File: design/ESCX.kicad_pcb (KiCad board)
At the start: 4 copper layers, 100 x 100 mm, 130 parts, among them J1 SWD, J10 Screw_Terminal_01x03, J11 Screw_Terminal_01x02, J2 Conn_Coaxial, J8 HALL_ENC, J9 USB_C_Receptacle_USB2.0_16P, Q1 IRF7854, Q2 IRF7854, Q3 IRF7854, Q4 IRF7854, Q5 IRF7854, Q6 IRF7854, SW1 SENSOR_VOLTAGE, U1 STM32F40X_LQFP64, U2 LM3671, U3 DRV8301, U4 nRF24L01P, U5 AD8418, U6 AD8418, U7 AD8418, X1 8MHz, X2 16MHz

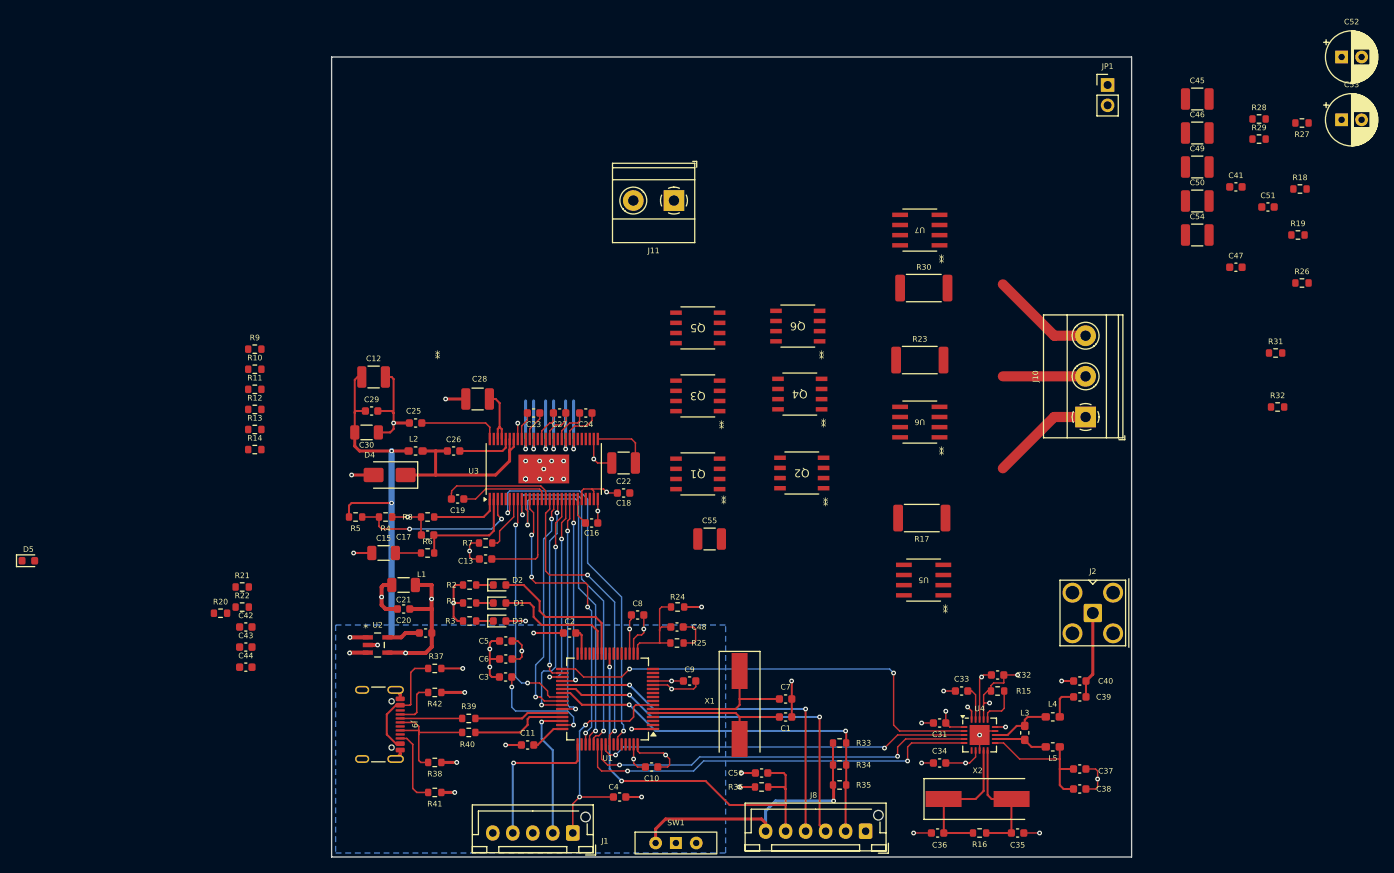
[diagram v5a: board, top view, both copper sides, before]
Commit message: Complete ruteo, menos plano GND2
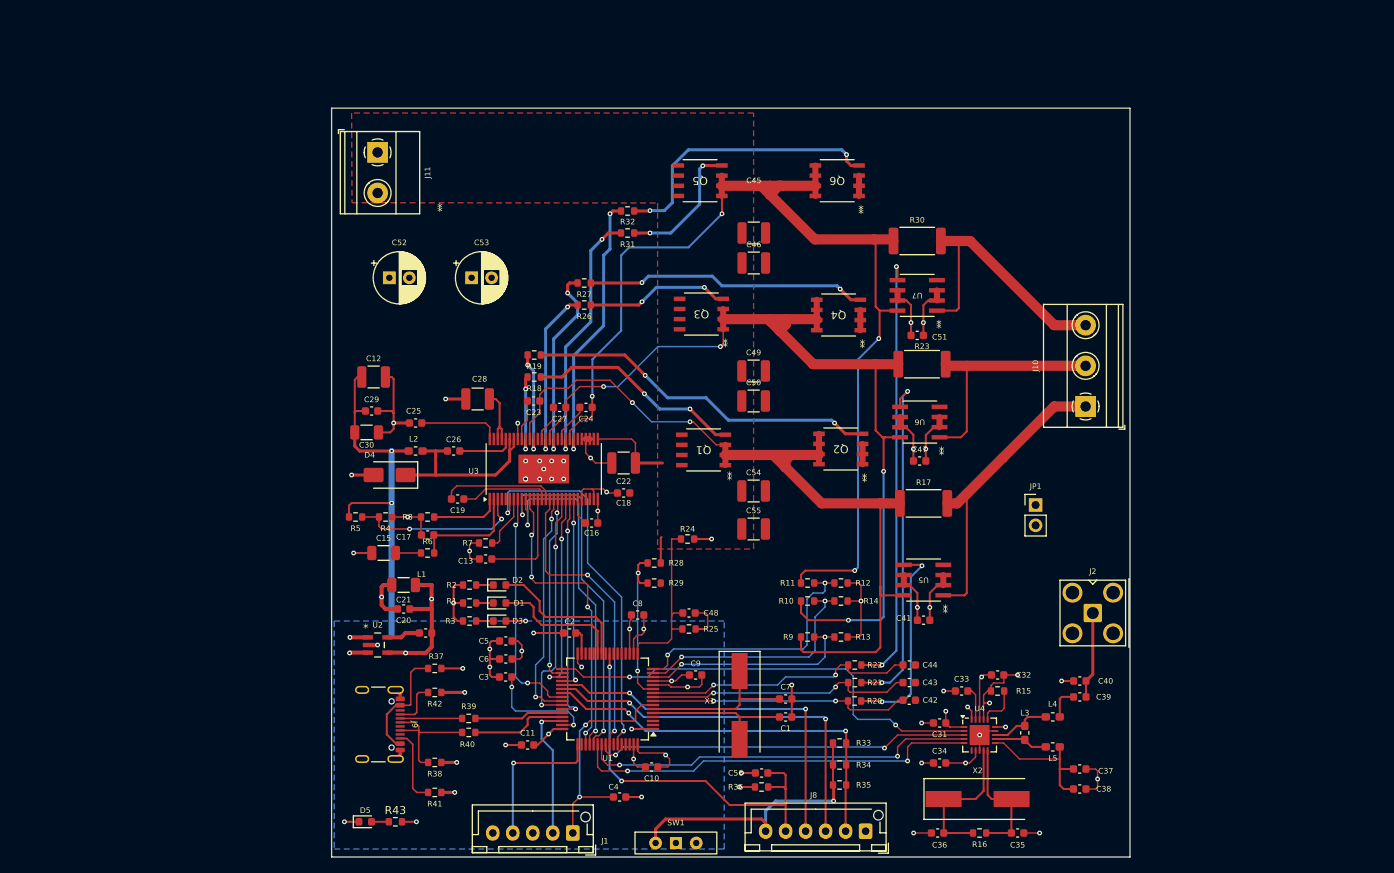
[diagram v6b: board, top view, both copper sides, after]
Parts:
- added R43: 150Ω, Resistor_SMD:R_0603_1608Metric, F.Cu at (107.0, 129.6)
- moved C52 122.2 mm to (106.2, 61.6)
- moved C53 110.5 mm to (116.5, 61.6)
- moved R18 98.6 mm to (124.3, 74.0), turned to 180 degrees
- moved R19 96.6 mm to (124.3, 71.2), turned to 180 degrees
- moved R28 93.8 mm to (139.3, 97.2), turned to 180 degrees
- moved R29 93.8 mm to (139.3, 99.8), turned to 180 degrees
- moved R27 91.9 mm to (130.6, 62.2)
- moved R26 89.8 mm to (130.6, 65.0), turned to 180 degrees
- moved R32 84.9 mm to (136.0, 53.2), turned to 180 degrees
- moved C42 83.4 mm to (171.2, 114.4)
- moved C43 83.0 mm to (171.2, 112.2)
- moved C44 82.9 mm to (171.2, 110.0)
- moved R31 82.4 mm to (136.0, 56.0), turned to 180 degrees
- moved R20 80.0 mm to (164.4, 114.5), turned to 180 degrees
- moved R9 77.9 mm to (158.5, 106.5)
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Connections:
- D5 pad 2: GND1 -> Net-(D5-A)
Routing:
- net /DRV8301/SH_C: track 5.27 -> 137.2 mm, vias 0 -> 4
- net /DRV8301/SH_B: track 4.51 -> 114.7 mm, vias 0 -> 4
- net /DRV8301/SH_A: track 3.77 -> 105.3 mm, vias 0 -> 2
- net /power/C_C: track 0.00 -> 54.9 mm, vias 0 -> 2
- net Net-(Q2-Pad1): track 0.00 -> 44.3 mm, vias 0 -> 2
- net /power/C_B: track 0.00 -> 43.2 mm, vias 0 -> 2
- net Net-(Q4-Pad1): track 0.00 -> 35.3 mm, vias 0 -> 2
- net Net-(Q6-Pad1): track 0.00 -> 35.2 mm, vias 0 -> 2
- net /MCU/CURRENT_3: track 0.00 -> 34.4 mm, vias 0 -> 2
- net /MCU/CURRENT_2: track 0.00 -> 33.6 mm, vias 0 -> 2
- net /DRV8301/SENS_C: track 0.00 -> 33.2 mm, vias 0 -> 2
- net /MCU/CURRENT_1: track 0.00 -> 32.7 mm, vias 0 -> 2
- net /DRV8301/SENS_B: track 0.00 -> 30.7 mm, vias 0 -> 2
- net GND2: track 4.76 -> 32.7 mm, vias 0 -> 3
- net /DRV8301/SENS_A: track 0.00 -> 27.6 mm, vias 0 -> 2
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- added copper zone on F.Cu, net SUPPLY
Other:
- board size 100 x 100 mm -> 99.8 x 93.6 mm

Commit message: Finalizado de ruteo de pcb
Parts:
- moved JP1 38.4 mm to (149.5, 98.2), turned to -90 degrees
- moved C51 4.80 mm to (177.0, 68.8)
- moved R30 4.80 mm to (177.0, 57.0)
- moved U7 4.80 mm to (177.0, 63.8)
- moved U6 4.54 mm to (177.1, 79.8)
- moved C47 4.54 mm to (177.0, 84.7)
- moved R23 4.54 mm to (177.3, 72.5)
- moved C41 4.50 mm to (177.5, 104.6)
- moved R17 4.50 mm to (177.5, 90.0)
- moved U5 4.50 mm to (177.5, 99.6)
- moved C52 2.91 mm to (109.0, 60.8)
- moved C53 2.91 mm to (119.3, 60.8)
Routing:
- net GND2: track 32.7 -> 109.3 mm, vias 3 -> 20
- net SUPPLY: track 21.8 -> 41.4 mm
- net /DRV8301/SH_C: track 137.2 -> 146.3 mm
- net GND1: track 158.1 -> 166.5 mm, vias 46 -> 47
- net /DRV8301/SH_B: track 114.7 -> 121.1 mm
- net /DRV8301/SH_A: track 105.3 -> 111.5 mm
- net /power/PH_C: track 33.8 -> 29.0 mm
- net /power/PH_B: track 29.5 -> 25.0 mm
- net /power/PH_A: track 37.7 -> 35.3 mm
- net /power/C_C: track 54.9 -> 57.3 mm
- net /power/C_B: track 43.2 -> 44.9 mm
- net /power/C_A: track 25.5 -> 27.3 mm
- net Net-(U3-AVDD): vias 1 -> 0
- added copper zone on In1.Cu, net GND2

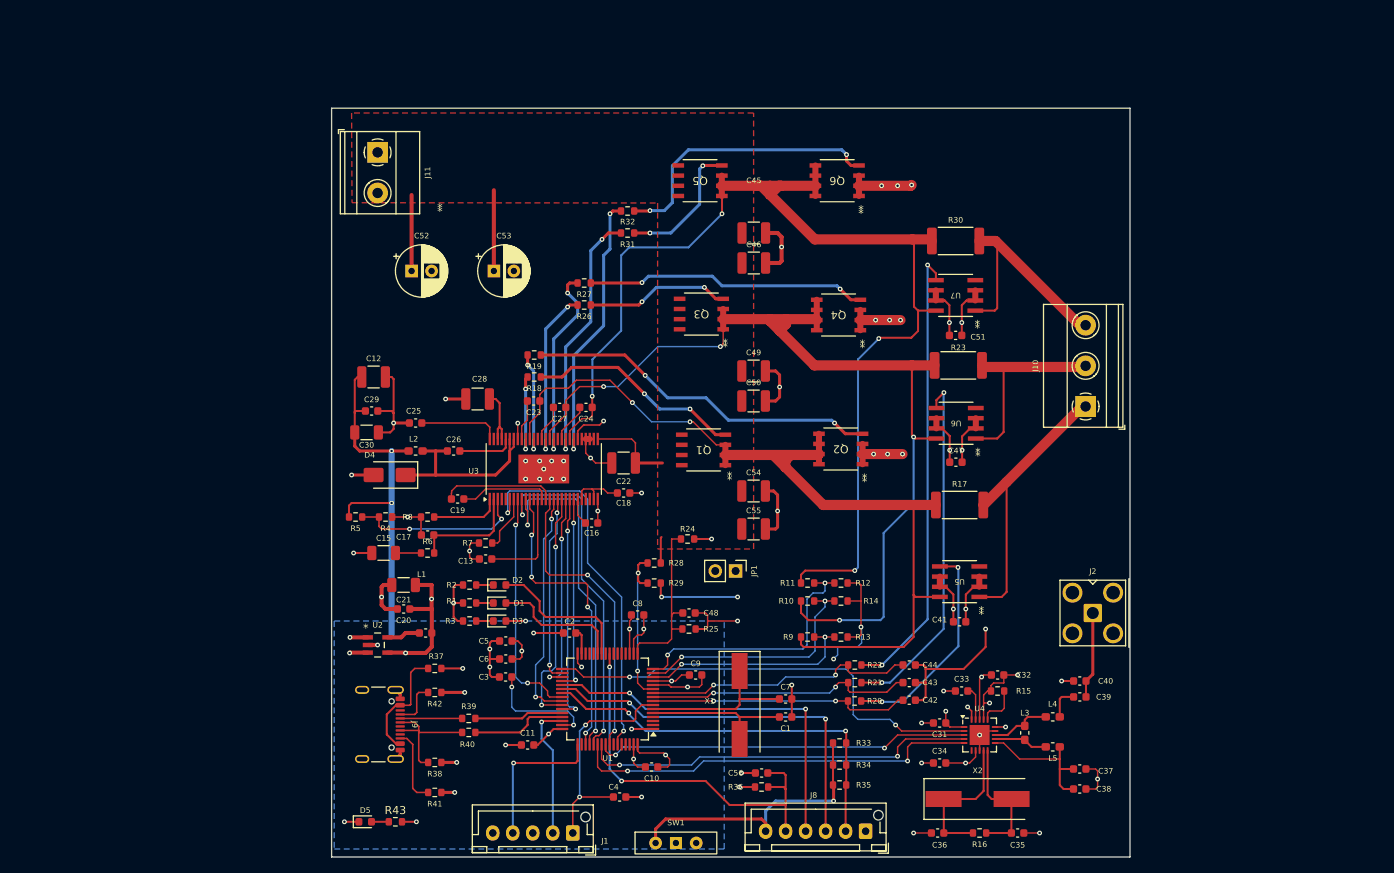
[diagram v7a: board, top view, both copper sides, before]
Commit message: Reubicacion de capacitores de entrada y mejora de ruteo
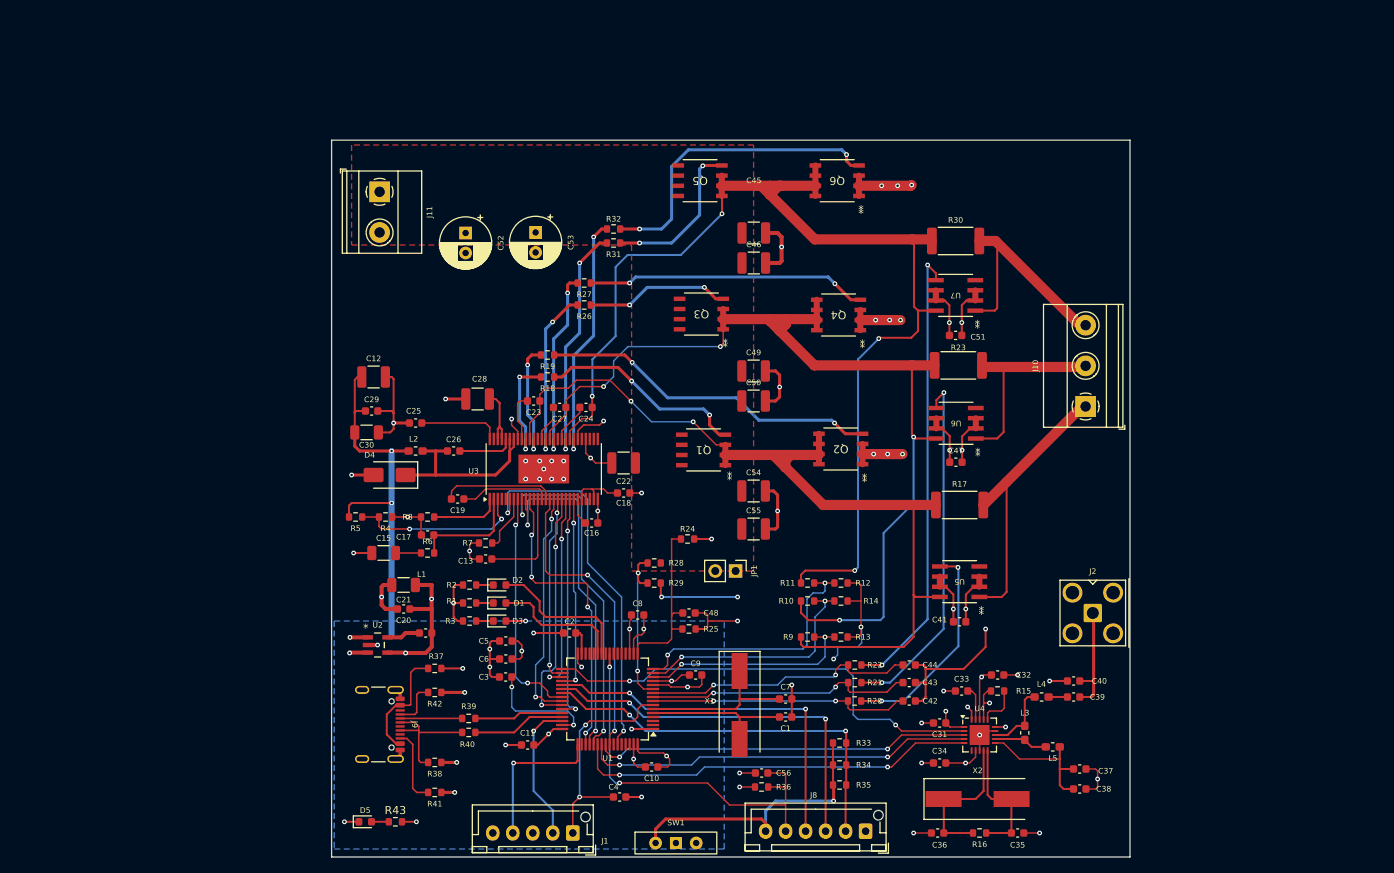
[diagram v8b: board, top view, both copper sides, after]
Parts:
- moved C52 8.25 mm to (115.8, 56.0), turned to -90 degrees
- moved C53 7.10 mm to (124.5, 55.9), turned to -90 degrees
- moved J11 4.94 mm to (105.0, 50.9)
- moved R32 2.85 mm to (134.2, 55.5)
- moved L4 2.85 mm to (187.8, 114.0)
- moved R31 2.15 mm to (134.2, 57.2)
- moved R18 1.67 mm to (126.0, 74.0)
- moved R19 1.67 mm to (126.0, 71.2)
- moved C39 0.78 mm to (191.8, 114.0)
- moved C40 0.78 mm to (191.8, 112.0)
- moved C42 0.10 mm to (171.2, 114.5)
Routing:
- net SUPPLY: track 41.4 -> 7.69 mm
- net GND1: track 166.5 -> 161.6 mm
- net Net-(Q6-Pad1): track 35.2 -> 39.1 mm
- net /DRV8301/GL_C: track 34.1 -> 30.9 mm
- net Net-(Q5-Pad1): track 17.0 -> 20.1 mm
- net Net-(J2-In): track 10.8 -> 13.9 mm
- net /DRV8301/GH_A: track 10.4 -> 13.2 mm
- net /DRV8301/GH_C: track 32.0 -> 29.7 mm
- net Net-(C39-Pad2): track 4.08 -> 2.35 mm
- net Net-(Q2-Pad1): track 44.3 -> 42.6 mm
- net /DRV8301/GL_A: track 13.3 -> 14.7 mm
- net /DRV8301/SH_B: track 121.1 -> 122.2 mm
- net Net-(U4-ANT2): track 7.71 -> 8.81 mm
- net /DRV8301/GL_B: track 24.9 -> 23.8 mm
- net Net-(U3-BST_A): track 5.04 -> 6.04 mm
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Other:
- board size 99.8 x 93.6 mm -> 99.8 x 89.6 mm
